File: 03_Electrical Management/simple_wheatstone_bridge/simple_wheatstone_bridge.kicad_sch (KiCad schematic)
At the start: 9 parts

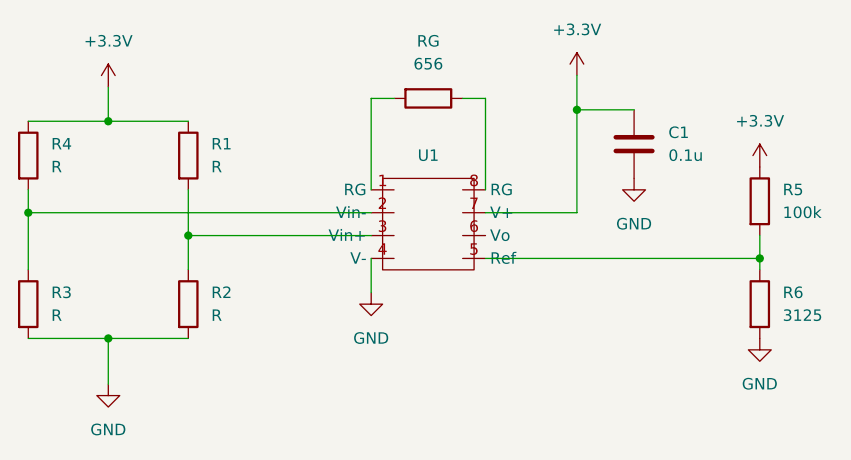
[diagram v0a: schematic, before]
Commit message: lead screw and amp pcb
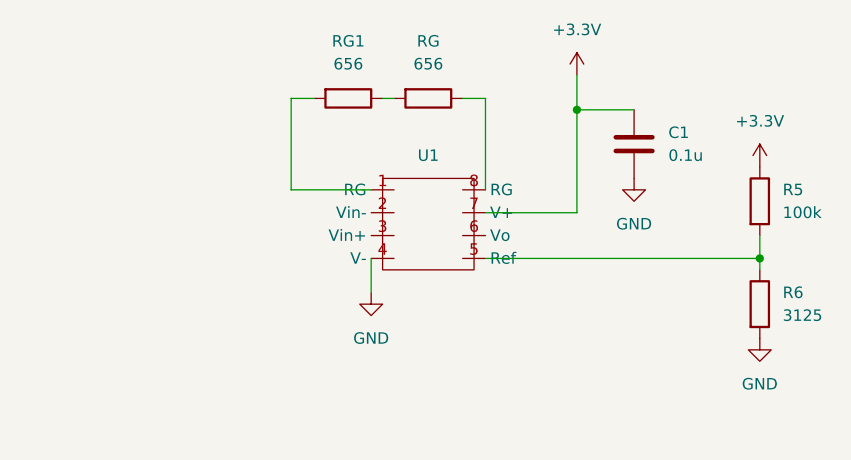
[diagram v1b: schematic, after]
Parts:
- removed R1, R2, R3, R4: R, symbol Device:R
- added RG1: 656, symbol Device:R
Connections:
- net at RG.2: now also RG1.1
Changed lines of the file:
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@@
   (junction (at 190.5 96.52) (diameter 0) (color 0 0 0 0)
   )
-  (junction (at 118.11 81.28) (diameter 0) (color 0 0 0 0)
-  )
-  (junction (at 109.22 91.44) (diameter 0) (color 0 0 0 0)
-  )
-  (junction (at 127 93.98) (diameter 0) (color 0 0 0 0)
-  )
-  (junction (at 118.11 105.41) (diameter 0) (color 0 0 0 0)
-  )
-  (wire (pts (xy 118.11 105.41) (xy 127 105.41))
-    (stroke (width 0) (type default))
-  )
   (wire (pts (xy 147.32 96.52) (xy 147.32 100.33))
     (stroke (width 0) (type default))
@@
     (stroke (width 0) (type default))
   )
-  (wire (pts (xy 109.22 91.44) (xy 109.22 97.79))
-    (stroke (width 0) (type default))
-  )
-  (wire (pts (xy 127 88.9) (xy 127 93.98))
+  (wire (pts (xy 147.32 88.9) (xy 138.43 88.9))
     (stroke (width 0) (type default))
   )
@@
     (stroke (width 0) (type default))
   )
-  (wire (pts (xy 127 93.98) (xy 147.32 93.98))
-    (stroke (width 0) (type default))
-  )
   (wire (pts (xy 190.5 96.52) (xy 190.5 97.79))
     (stroke (width 0) (type default))
@@
     (stroke (width 0) (type default))
   )
-  (wire (pts (xy 109.22 105.41) (xy 118.11 105.41))
-    (stroke (width 0) (type default))
-  )
-  (wire (pts (xy 109.22 91.44) (xy 147.32 91.44))
-    (stroke (width 0) (type default))
-  )
   (wire (pts (xy 170.18 91.44) (xy 160.02 91.44))
     (stroke (width 0) (type default))
@@
     (stroke (width 0) (type default))
   )
-  (wire (pts (xy 147.32 88.9) (xy 147.32 78.74))
-    (stroke (width 0) (type default))
-  )
-  (wire (pts (xy 109.22 88.9) (xy 109.22 91.44))
+  (wire (pts (xy 138.43 88.9) (xy 138.43 78.74))
     (stroke (width 0) (type default))
   )
@@
     (stroke (width 0) (type default))
   )
-  (wire (pts (xy 127 93.98) (xy 127 97.79))
-    (stroke (width 0) (type default))
-  )
-  (wire (pts (xy 109.22 81.28) (xy 118.11 81.28))
-    (stroke (width 0) (type default))
-  )
-  (wire (pts (xy 118.11 77.47) (xy 118.11 81.28))
-    (stroke (width 0) (type default))
-  )
-  (wire (pts (xy 118.11 81.28) (xy 127 81.28))
-    (stroke (width 0) (type default))
-  )
-  (wire (pts (xy 118.11 105.41) (xy 118.11 110.49))
-    (stroke (width 0) (type default))
-  )
-  (wire (pts (xy 147.32 78.74) (xy 149.86 78.74))
-    (stroke (width 0) (type default))
-  )
-  (symbol (lib_id "Device:R") (at 127 85.09 0) (unit 1)
-    (in_bom yes) (on_board yes) (dnp no) (fields_autoplaced)
-    (property "Reference" "R1" (at 129.54 83.82 0)
-      (effects (font (size 1.27 1.27)) (justify left))
-    )
-    (property "Value" "R" (at 129.54 86.36 0)
-      (effects (font (size 1.27 1.27)) (justify left))
-    )
-    (property "Footprint" "" (at 125.222 85.09 90)
-      (effects (font (size 1.27 1.27)) hide)
-    )
-    (property "Datasheet" "~" (at 127 85.09 0)
-      (effects (font (size 1.27 1.27)) hide)
-    )
-    (pin "2")
-    (pin "1")
-    (instances
-      (project "simple_wheatstone_bridge"
-        (path "/a17f448e-e1e1-44a8-a24d-b5b63a0b8b5e"
-          (reference "R1") (unit 1)
-        )
-      )
-    )
+  (wire (pts (xy 138.43 78.74) (xy 140.97 78.74))
+    (stroke (width 0) (type default))
+  )
+  (wire (pts (xy 148.59 78.74) (xy 149.86 78.74))
+    (stroke (width 0) (type default))
   )
   (symbol (lib_id "power:GND") (at 190.5 105.41 0) (unit 1)
@@
         (path "/a17f448e-e1e1-44a8-a24d-b5b63a0b8b5e"
           (reference "C1") (unit 1)
-        )
-      )
-    )
-  )
-  (symbol (lib_id "Device:R") (at 109.22 85.09 0) (unit 1)
-    (in_bom yes) (on_board yes) (dnp no) (fields_autoplaced)
-    (property "Reference" "R4" (at 111.76 83.82 0)
-      (effects (font (size 1.27 1.27)) (justify left))
-    )
-    (property "Value" "R" (at 111.76 86.36 0)
-      (effects (font (size 1.27 1.27)) (justify left))
-    )
-    (property "Footprint" "" (at 107.442 85.09 90)
-      (effects (font (size 1.27 1.27)) hide)
-    )
-    (property "Datasheet" "~" (at 109.22 85.09 0)
-      (effects (font (size 1.27 1.27)) hide)
-    )
-    (pin "1")
-    (pin "2")
-    (instances
-      (project "simple_wheatstone_bridge"
-        (path "/a17f448e-e1e1-44a8-a24d-b5b63a0b8b5e"
-          (reference "R4") (unit 1)
         )
       )
@@
     )
   )
-  (symbol (lib_id "power:+3.3V") (at 118.11 77.47 0) (unit 1)
-    (in_bom yes) (on_board yes) (dnp no) (fields_autoplaced)
-    (property "Reference" "#PWR01" (at 118.11 81.28 0)
-      (effects (font (size 1.27 1.27)) hide)
-    )
-    (property "Value" "+3.3V" (at 118.11 72.39 0)
-      (effects (font (size 1.27 1.27)))
-    )
-    (property "Footprint" "" (at 118.11 77.47 0)
-      (effects (font (size 1.27 1.27)) hide)
-    )
-    (property "Datasheet" "" (at 118.11 77.47 0)
-      (effects (font (size 1.27 1.27)) hide)
-    )
-    (pin "1")
-    (instances
-      (project "simple_wheatstone_bridge"
-        (path "/a17f448e-e1e1-44a8-a24d-b5b63a0b8b5e"
-          (reference "#PWR01") (unit 1)
-        )
-      )
-    )
-  )
   (symbol (lib_id "power:GND") (at 176.53 87.63 0) (unit 1)
     (in_bom yes) (on_board yes) (dnp no) (fields_autoplaced)
@@
     )
   )
-  (symbol (lib_id "Device:R") (at 109.22 101.6 0) (unit 1)
-    (in_bom yes) (on_board yes) (dnp no) (fields_autoplaced)
-    (property "Reference" "R3" (at 111.76 100.33 0)
-      (effects (font (size 1.27 1.27)) (justify left))
-    )
-    (property "Value" "R" (at 111.76 102.87 0)
-      (effects (font (size 1.27 1.27)) (justify left))
-    )
-    (property "Footprint" "" (at 107.442 101.6 90)
-      (effects (font (size 1.27 1.27)) hide)
-    )
-    (property "Datasheet" "~" (at 109.22 101.6 0)
-      (effects (font (size 1.27 1.27)) hide)
-    )
-    (pin "2")
-    (pin "1")
-    (instances
-      (project "simple_wheatstone_bridge"
-        (path "/a17f448e-e1e1-44a8-a24d-b5b63a0b8b5e"
-          (reference "R3") (unit 1)
-        )
-      )
-    )
-  )
   (symbol (lib_id "power:GND") (at 147.32 100.33 0) (unit 1)
     (in_bom yes) (on_board yes) (dnp no) (fields_autoplaced)
@@
     )
   )
+  (symbol (lib_id "Device:R") (at 144.78 78.74 270) (unit 1)
+    (in_bom yes) (on_board yes) (dnp no) (fields_autoplaced)
+    (property "Reference" "RG1" (at 144.78 72.39 90)
+      (effects (font (size 1.27 1.27)))
+    )
+    (property "Value" "656" (at 144.78 74.93 90)
+      (effects (font (size 1.27 1.27)))
+    )
+    (property "Footprint" "" (at 144.78 76.962 90)
+      (effects (font (size 1.27 1.27)) hide)
+    )
+    (property "Datasheet" "~" (at 144.78 78.74 0)
+      (effects (font (size 1.27 1.27)) hide)
+    )
+    (pin "1")
+    (pin "2")
+    (instances
+      (project "simple_wheatstone_bridge"
+        (path "/a17f448e-e1e1-44a8-a24d-b5b63a0b8b5e"
+          (reference "RG1") (unit 1)
+        )
+      )
+    )
+  )
   (symbol (lib_id "Device:R") (at 190.5 90.17 0) (unit 1)
     (in_bom yes) (on_board yes) (dnp no) (fields_autoplaced)
@@
         )
       )
-    )
-  )
-  (symbol (lib_id "power:GND") (at 118.11 110.49 0) (unit 1)
-    (in_bom yes) (on_board yes) (dnp no) (fields_autoplaced)
-    (property "Reference" "#PWR02" (at 118.11 116.84 0)
-      (effects (font (size 1.27 1.27)) hide)
-    )
-    (property "Value" "GND" (at 118.11 115.57 0)
-      (effects (font (size 1.27 1.27)))
-    )
-    (property "Footprint" "" (at 118.11 110.49 0)
-      (effects (font (size 1.27 1.27)) hide)
-    )
-    (property "Datasheet" "" (at 118.11 110.49 0)
-      (effects (font (size 1.27 1.27)) hide)
-    )
-    (pin "1")
-    (instances
-      (project "simple_wheatstone_bridge"
-        (path "/a17f448e-e1e1-44a8-a24d-b5b63a0b8b5e"
-          (reference "#PWR02") (unit 1)
-        )
-      )
-    )
-  )
-  (symbol (lib_id "Device:R") (at 127 101.6 0) (unit 1)
-    (in_bom yes) (on_board yes) (dnp no) (fields_autoplaced)
-    (property "Reference" "R2" (at 129.54 100.33 0)
-      (effects (font (size 1.27 1.27)) (justify left))
-    )
-    (property "Value" "R" (at 129.54 102.87 0)
-      (effects (font (size 1.27 1.27)) (justify left))
-    )
-    (property "Footprint" "" (at 125.222 101.6 90)
-      (effects (font (size 1.27 1.27)) hide)
-    )
-    (property "Datasheet" "~" (at 127 101.6 0)
-      (effects (font (size 1.27 1.27)) hide)
-    )
-    (pin "1")
-    (pin "2")
-    (instances
-      (project "simple_wheatstone_bridge"
-        (path "/a17f448e-e1e1-44a8-a24d-b5b63a0b8b5e"
-          (reference "R2") (unit 1)
-        )
-      )
